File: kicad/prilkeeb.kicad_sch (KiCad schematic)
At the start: 71 parts, among them U2 Nice_Nano_V2

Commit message: Update layout
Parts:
- renumbered S3 to S1, S12 to S10, S13 to S11, S8 to S12, S9 to S13, S17 to S15, S18 to S16, S19 to S17, S20 to S18, S15 to S19, S4 to S2, S16 to S20, S24 to S22, S25 to S23, S26 to S24, S27 to S25, S22 to S26, S23 to S27, S5 to S3, S35 to S33, S33 to S35, S6 to S4, S1 to S5, S2 to S6, S10 to S8, S11 to S9
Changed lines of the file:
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@@
 		(dnp no)
 		(fields_autoplaced yes)
-		(property "Reference" "S5"
+		(property "Reference" "S3"
 			(at 96.52 73.66 0)
 			(do_not_autoplace yes)
@@
 			(project "nhienkeeb"
 				(path "/f238781f-c890-404f-bc9e-87ff6761e41b"
-					(reference "S5")
+					(reference "S3")
 					(unit 1)
 				)
@@
 		(dnp no)
 		(fields_autoplaced yes)
-		(property "Reference" "S6"
+		(property "Reference" "S4"
 			(at 111.76 73.66 0)
 			(do_not_autoplace yes)
@@
 			(project "nhienkeeb"
 				(path "/f238781f-c890-404f-bc9e-87ff6761e41b"
-					(reference "S6")
+					(reference "S4")
 					(unit 1)
 				)
@@
 		(dnp no)
 		(fields_autoplaced yes)
-		(property "Reference" "S24"
+		(property "Reference" "S22"
 			(at 67.31 119.38 0)
 			(do_not_autoplace yes)
@@
 			(project "nhienkeeb"
 				(path "/f238781f-c890-404f-bc9e-87ff6761e41b"
-					(reference "S24")
+					(reference "S22")
 					(unit 1)
 				)
@@
 		(dnp no)
 		(fields_autoplaced yes)
-		(property "Reference" "S22"
+		(property "Reference" "S26"
 			(at 39.37 119.38 0)
 			(do_not_autoplace yes)
@@
 			(project "nhienkeeb"
 				(path "/f238781f-c890-404f-bc9e-87ff6761e41b"
-					(reference "S22")
+					(reference "S26")
 					(unit 1)
 				)
@@
 		(on_board yes)
 		(dnp no)
-		(property "Reference" "S9"
+		(property "Reference" "S13"
 			(at 53.34 88.9 0)
 			(do_not_autoplace yes)
@@
 			(project "nhienkeeb"
 				(path "/f238781f-c890-404f-bc9e-87ff6761e41b"
-					(reference "S9")
+					(reference "S13")
 					(unit 1)
 				)
@@
 		(dnp no)
 		(fields_autoplaced yes)
-		(property "Reference" "S13"
+		(property "Reference" "S11"
 			(at 111.76 88.9 0)
 			(do_not_autoplace yes)
@@
 			(project "nhienkeeb"
 				(path "/f238781f-c890-404f-bc9e-87ff6761e41b"
-					(reference "S13")
+					(reference "S11")
 					(unit 1)
 				)
@@
 		(dnp no)
 		(fields_autoplaced yes)
-		(property "Reference" "S33"
+		(property "Reference" "S35"
 			(at 96.52 134.62 0)
 			(do_not_autoplace yes)
@@
 			(project "nhienkeeb"
 				(path "/f238781f-c890-404f-bc9e-87ff6761e41b"
-					(reference "S33")
+					(reference "S35")
 					(unit 1)
 				)
@@
 		(dnp no)
 		(fields_autoplaced yes)
-		(property "Reference" "S4"
+		(property "Reference" "S2"
 			(at 81.28 73.66 0)
 			(do_not_autoplace yes)
@@
 			(project "nhienkeeb"
 				(path "/f238781f-c890-404f-bc9e-87ff6761e41b"
-					(reference "S4")
+					(reference "S2")
 					(unit 1)
 				)
@@
 		(dnp no)
 		(fields_autoplaced yes)
-		(property "Reference" "S8"
+		(property "Reference" "S12"
 			(at 39.37 88.9 0)
 			(do_not_autoplace yes)
@@
 			(project "nhienkeeb"
 				(path "/f238781f-c890-404f-bc9e-87ff6761e41b"
-					(reference "S8")
+					(reference "S12")
 					(unit 1)
 				)
@@
 		(dnp no)
 		(fields_autoplaced yes)
-		(property "Reference" "S20"
+		(property "Reference" "S18"
 			(at 111.76 104.14 0)
 			(do_not_autoplace yes)
@@
 			(project "nhienkeeb"
 				(path "/f238781f-c890-404f-bc9e-87ff6761e41b"
-					(reference "S20")
+					(reference "S18")
 					(unit 1)
 				)
@@
 		(dnp no)
 		(fields_autoplaced yes)
-		(property "Reference" "S18"
+		(property "Reference" "S16"
 			(at 81.28 104.14 0)
 			(do_not_autoplace yes)
@@
 			(project "nhienkeeb"
 				(path "/f238781f-c890-404f-bc9e-87ff6761e41b"
-					(reference "S18")
+					(reference "S16")
 					(unit 1)
 				)
@@
 		(dnp no)
 		(fields_autoplaced yes)
-		(property "Reference" "S10"
+		(property "Reference" "S8"
 			(at 67.31 88.9 0)
 			(do_not_autoplace yes)
@@
 			(project "nhienkeeb"
 				(path "/f238781f-c890-404f-bc9e-87ff6761e41b"
-					(reference "S10")
+					(reference "S8")
 					(unit 1)
 				)
@@
 		(dnp no)
 		(fields_autoplaced yes)
-		(property "Reference" "S35"
+		(property "Reference" "S33"
 			(at 125.73 134.62 0)
 			(do_not_autoplace yes)
@@
 			(project "nhienkeeb"
 				(path "/f238781f-c890-404f-bc9e-87ff6761e41b"
-					(reference "S35")
+					(reference "S33")
 					(unit 1)
 				)
@@
 		(on_board yes)
 		(dnp no)
-		(property "Reference" "S23"
+		(property "Reference" "S27"
 			(at 53.34 119.38 0)
 			(do_not_autoplace yes)
@@
 			(project "nhienkeeb"
 				(path "/f238781f-c890-404f-bc9e-87ff6761e41b"
-					(reference "S23")
+					(reference "S27")
 					(unit 1)
 				)
@@
 		(dnp no)
 		(fields_autoplaced yes)
-		(property "Reference" "S17"
+		(property "Reference" "S15"
 			(at 67.31 104.14 0)
 			(do_not_autoplace yes)
@@
 			(project "nhienkeeb"
 				(path "/f238781f-c890-404f-bc9e-87ff6761e41b"
-					(reference "S17")
+					(reference "S15")
 					(unit 1)
 				)
@@
 		(dnp no)
 		(fields_autoplaced yes)
-		(property "Reference" "S12"
+		(property "Reference" "S10"
 			(at 96.52 88.9 0)
 			(do_not_autoplace yes)
@@
 			(project "nhienkeeb"
 				(path "/f238781f-c890-404f-bc9e-87ff6761e41b"
-					(reference "S12")
+					(reference "S10")
 					(unit 1)
 				)
@@
 		(dnp no)
 		(fields_autoplaced yes)
-		(property "Reference" "S25"
+		(property "Reference" "S23"
 			(at 81.28 119.38 0)
 			(do_not_autoplace yes)
@@
 			(project "nhienkeeb"
 				(path "/f238781f-c890-404f-bc9e-87ff6761e41b"
-					(reference "S25")
+					(reference "S23")
 					(unit 1)
 				)
@@
 		(on_board yes)
 		(dnp no)
-		(property "Reference" "S16"
+		(property "Reference" "S20"
 			(at 53.34 104.14 0)
 			(do_not_autoplace yes)
@@
 			(project "nhienkeeb"
 				(path "/f238781f-c890-404f-bc9e-87ff6761e41b"
-					(reference "S16")
+					(reference "S20")
 					(unit 1)
 				)
@@
 		(dnp no)
 		(fields_autoplaced yes)
-		(property "Reference" "S15"
+		(property "Reference" "S19"
 			(at 39.37 104.14 0)
 			(do_not_autoplace yes)
@@
 			(project "nhienkeeb"
 				(path "/f238781f-c890-404f-bc9e-87ff6761e41b"
-					(reference "S15")
+					(reference "S19")
 					(unit 1)
 				)
@@
 		(dnp no)
 		(fields_autoplaced yes)
-		(property "Reference" "S27"
+		(property "Reference" "S25"
 			(at 111.76 119.38 0)
 			(do_not_autoplace yes)
@@
 			(project "nhienkeeb"
 				(path "/f238781f-c890-404f-bc9e-87ff6761e41b"
-					(reference "S27")
+					(reference "S25")
 					(unit 1)
 				)
@@
 		(dnp no)
 		(fields_autoplaced yes)
-		(property "Reference" "S1"
+		(property "Reference" "S5"
 			(at 39.37 73.66 0)
 			(do_not_autoplace yes)
@@
 			(project ""
 				(path "/f238781f-c890-404f-bc9e-87ff6761e41b"
-					(reference "S1")
+					(reference "S5")
 					(unit 1)
 				)
@@
 		(dnp no)
 		(fields_autoplaced yes)
-		(property "Reference" "S19"
+		(property "Reference" "S17"
 			(at 96.52 104.14 0)
 			(do_not_autoplace yes)
@@
 			(project "nhienkeeb"
 				(path "/f238781f-c890-404f-bc9e-87ff6761e41b"
-					(reference "S19")
+					(reference "S17")
 					(unit 1)
 				)
@@
 		(dnp no)
 		(fields_autoplaced yes)
-		(property "Reference" "S3"
+		(property "Reference" "S1"
 			(at 67.31 73.66 0)
 			(do_not_autoplace yes)
@@
 			(project "nhienkeeb"
 				(path "/f238781f-c890-404f-bc9e-87ff6761e41b"
-					(reference "S3")
+					(reference "S1")
 					(unit 1)
 				)
@@
 		(dnp no)
 		(fields_autoplaced yes)
-		(property "Reference" "S26"
+		(property "Reference" "S24"
 			(at 96.52 119.38 0)
 			(do_not_autoplace yes)
@@
 			(project "nhienkeeb"
 				(path "/f238781f-c890-404f-bc9e-87ff6761e41b"
-					(reference "S26")
+					(reference "S24")
 					(unit 1)
 				)
@@
 		(dnp no)
 		(fields_autoplaced yes)
-		(property "Reference" "S11"
+		(property "Reference" "S9"
 			(at 81.28 88.9 0)
 			(do_not_autoplace yes)
@@
 			(project "nhienkeeb"
 				(path "/f238781f-c890-404f-bc9e-87ff6761e41b"
-					(reference "S11")
+					(reference "S9")
 					(unit 1)
 				)
@@
 		(on_board yes)
 		(dnp no)
-		(property "Reference" "S2"
+		(property "Reference" "S6"
 			(at 53.34 73.66 0)
 			(do_not_autoplace yes)
@@
 			(project "nhienkeeb"
 				(path "/f238781f-c890-404f-bc9e-87ff6761e41b"
-					(reference "S2")
+					(reference "S6")
 					(unit 1)
 				)

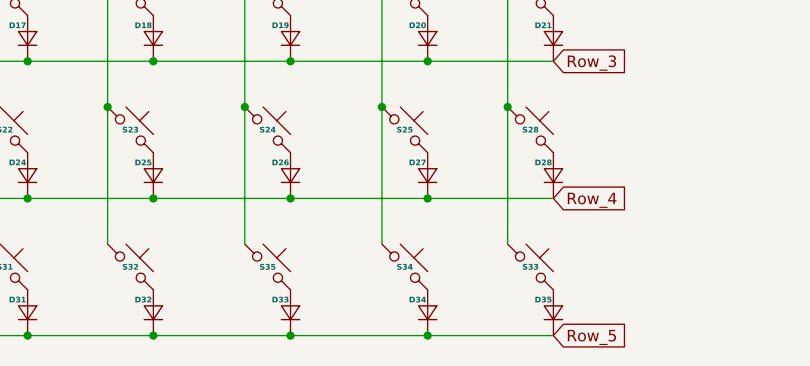
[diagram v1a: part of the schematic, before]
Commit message: Update placement and basice routing
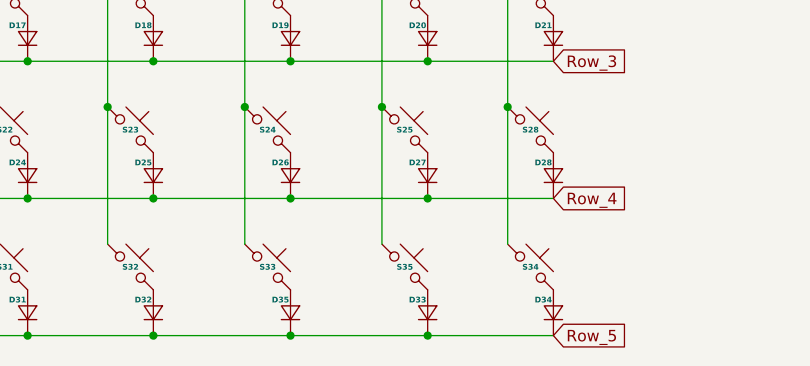
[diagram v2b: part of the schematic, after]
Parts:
- renumbered D34 to D33, D35 to D34, D33 to D35, S35 to S33, S33 to S34, S34 to S35
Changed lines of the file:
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@@
 		(dnp no)
 		(fields_autoplaced yes)
-		(property "Reference" "D34"
+		(property "Reference" "D33"
 			(at 114.15 138.634 0)
 			(do_not_autoplace yes)
@@
 			(project "nhienkeeb"
 				(path "/f238781f-c890-404f-bc9e-87ff6761e41b"
-					(reference "D34")
+					(reference "D33")
 					(unit 1)
 				)
@@
 		(dnp no)
 		(fields_autoplaced yes)
-		(property "Reference" "S35"
+		(property "Reference" "S33"
 			(at 96.52 134.62 0)
 			(do_not_autoplace yes)
@@
 			(project "nhienkeeb"
 				(path "/f238781f-c890-404f-bc9e-87ff6761e41b"
-					(reference "S35")
+					(reference "S33")
 					(unit 1)
 				)
@@
 		(dnp no)
 		(fields_autoplaced yes)
-		(property "Reference" "S33"
+		(property "Reference" "S34"
 			(at 125.73 134.62 0)
 			(do_not_autoplace yes)
@@
 			(project "nhienkeeb"
 				(path "/f238781f-c890-404f-bc9e-87ff6761e41b"
-					(reference "S33")
+					(reference "S34")
 					(unit 1)
 				)
@@
 		(dnp no)
 		(fields_autoplaced yes)
-		(property "Reference" "S34"
+		(property "Reference" "S35"
 			(at 111.76 134.62 0)
 			(do_not_autoplace yes)
@@
 			(project "nhienkeeb"
 				(path "/f238781f-c890-404f-bc9e-87ff6761e41b"
-					(reference "S34")
+					(reference "S35")
 					(unit 1)
 				)
@@
 		(dnp no)
 		(fields_autoplaced yes)
-		(property "Reference" "D33"
+		(property "Reference" "D35"
 			(at 98.91 138.634 0)
 			(do_not_autoplace yes)
@@
 			(project "nhienkeeb"
 				(path "/f238781f-c890-404f-bc9e-87ff6761e41b"
-					(reference "D33")
+					(reference "D35")
 					(unit 1)
 				)
@@
 		(dnp no)
 		(fields_autoplaced yes)
-		(property "Reference" "D35"
+		(property "Reference" "D34"
 			(at 128.12 138.634 0)
 			(do_not_autoplace yes)
@@
 			(project "nhienkeeb"
 				(path "/f238781f-c890-404f-bc9e-87ff6761e41b"
-					(reference "D35")
-					(unit 1)
-				)
+					(reference "D34")
+					(unit 1)
+				)

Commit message: Update layout
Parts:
- renumbered S35 to S32, S34 to S33, S32 to S34, S33 to S35
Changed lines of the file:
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@@
 		(dnp no)
 		(fields_autoplaced yes)
-		(property "Reference" "S33"
+		(property "Reference" "S35"
 			(at 96.52 134.62 0)
 			(do_not_autoplace yes)
@@
 			(project "nhienkeeb"
 				(path "/f238781f-c890-404f-bc9e-87ff6761e41b"
-					(reference "S33")
+					(reference "S35")
 					(unit 1)
 				)
@@
 		(dnp no)
 		(fields_autoplaced yes)
-		(property "Reference" "S34"
+		(property "Reference" "S33"
 			(at 125.73 134.62 0)
 			(do_not_autoplace yes)
@@
 			(project "nhienkeeb"
 				(path "/f238781f-c890-404f-bc9e-87ff6761e41b"
-					(reference "S34")
+					(reference "S33")
 					(unit 1)
 				)
@@
 		(dnp no)
 		(fields_autoplaced yes)
-		(property "Reference" "S35"
+		(property "Reference" "S32"
 			(at 111.76 134.62 0)
 			(do_not_autoplace yes)
@@
 			(project "nhienkeeb"
 				(path "/f238781f-c890-404f-bc9e-87ff6761e41b"
-					(reference "S35")
+					(reference "S32")
 					(unit 1)
 				)
@@
 		(dnp no)
 		(fields_autoplaced yes)
-		(property "Reference" "S32"
+		(property "Reference" "S34"
 			(at 81.28 134.62 0)
 			(do_not_autoplace yes)
@@
 			(project "nhienkeeb"
 				(path "/f238781f-c890-404f-bc9e-87ff6761e41b"
-					(reference "S32")
-					(unit 1)
-				)
+					(reference "S34")
+					(unit 1)
+				)

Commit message: Update layout
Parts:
- renumbered S35 to S32, S32 to S33, S33 to S34, S34 to S35
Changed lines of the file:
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@@
 		(dnp no)
 		(fields_autoplaced yes)
-		(property "Reference" "S35"
+		(property "Reference" "S32"
 			(at 96.52 134.62 0)
 			(do_not_autoplace yes)
@@
 			(project "nhienkeeb"
 				(path "/f238781f-c890-404f-bc9e-87ff6761e41b"
-					(reference "S35")
+					(reference "S32")
 					(unit 1)
 				)
@@
 		(dnp no)
 		(fields_autoplaced yes)
-		(property "Reference" "S33"
+		(property "Reference" "S34"
 			(at 125.73 134.62 0)
 			(do_not_autoplace yes)
@@
 			(project "nhienkeeb"
 				(path "/f238781f-c890-404f-bc9e-87ff6761e41b"
-					(reference "S33")
+					(reference "S34")
 					(unit 1)
 				)
@@
 		(dnp no)
 		(fields_autoplaced yes)
-		(property "Reference" "S32"
+		(property "Reference" "S33"
 			(at 111.76 134.62 0)
 			(do_not_autoplace yes)
@@
 			(project "nhienkeeb"
 				(path "/f238781f-c890-404f-bc9e-87ff6761e41b"
-					(reference "S32")
+					(reference "S33")
 					(unit 1)
 				)
@@
 		(dnp no)
 		(fields_autoplaced yes)
-		(property "Reference" "S34"
+		(property "Reference" "S35"
 			(at 81.28 134.62 0)
 			(do_not_autoplace yes)
@@
 			(project "nhienkeeb"
 				(path "/f238781f-c890-404f-bc9e-87ff6761e41b"
-					(reference "S34")
-					(unit 1)
-				)
+					(reference "S35")
+					(unit 1)
+				)

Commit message: Update design
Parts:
- added RST_SW_L1, RST_SW_R1: SW_Push, Button_Switch_SMD:SW_SPST_SKQG_WithStem, symbol Switch:SW_Push
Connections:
- net VCC: now reaches U2.21 (3.3v)
- net RST: now reaches U2.22 (RST)
- net RST: now also RST_SW_L1.2, RST_SW_R1.2
- net GND: now reaches U2.23 (GND)
- net GND: now also RST_SW_L1.1, RST_SW_R1.1

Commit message: Design checkpoint
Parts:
- removed RST_SW_R1: SW_Push, Button_Switch_SMD:SW_SPST_SKQG_WithStem, symbol Switch:SW_Push
- removed S34: S35, key-switches:SW_MX_HotSwap_PTH_double, symbol ScottoKeebs:Placeholder_Keyswitch
- added BT1: Battery_Cell, dumta:Battery_pads_reversible, symbol Device:Battery_Cell
- added ROT1: RotaryEncoder_Switch_MP, ScottoKeebs_Scotto:Encoder_EC11_MX, symbol Device:RotaryEncoder_Switch_MP
- added SW1: SW_SPDT, dumta:power_switch_padreverse, symbol Switch:SW_SPDT
- RST_SW1: renamed from RST_SW_L1; footprint Button_Switch_SMD:SW_SPST_SKQG_WithStem -> Button_Switch_THT:SW_PUSH_6mm_H4.3mm
- renumbered D35 to D33, D33 to D34, D34 to DROTARY1, S35 to S34
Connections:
- net Col_7: now also ROT1.S2
- net RotaryA: now reaches U2.11 (8)
- net RotaryA: now also ROT1.A
- net RotaryB: now reaches U2.12 (9)
- net RotaryB: now also ROT1.B
- net at DROTARY1.2 (A): now also ROT1.S1
- new net: BT1.1 (+), SW1.2 (B)
- new net B+: SW1.3 (C), U2.29 (B+)
- new net B-: BT1.2 (-), U2.28 (B-)

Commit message: Update components
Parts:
- added RST_SW2: SW_Push, ScottoKeebs_Components:Button_TL3342, symbol Switch:SW_Push
- ROT1: footprint ScottoKeebs_Scotto:Encoder_EC11_MX -> prillkeeb:Encoder_EC11_MX_Jumpers_Reversible
- RST_SW1: footprint Button_Switch_THT:SW_PUSH_6mm_H4.3mm -> ScottoKeebs_Components:Button_TL3342
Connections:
- net GND: now also RST_SW2.1
- net RST: now also RST_SW2.2
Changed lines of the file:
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@@
 		)
 	)
+	(global_label "RST"
+		(shape input)
+		(at 200.66 68.58 0)
+		(fields_autoplaced yes)
+		(effects
+			(font
+				(size 1.27 1.27)
+			)
+			(justify left)
+		)
+		(property "Intersheetrefs" "${INTERSHEET_REFS}"
+			(at 207.0923 68.58 0)
+			(effects
+				(font
+					(size 1.27 1.27)
+				)
+				(justify left)
+				(hide yes)
+			)
+		)
+	)
 	(global_label "Col_5"
 		(shape input)
@@
 		)
 	)
+	(global_label "GND"
+		(shape input)
+		(at 190.5 68.58 180)
+		(fields_autoplaced yes)
+		(effects
+			(font
+				(size 1.27 1.27)
+			)
+			(justify right)
+		)
+		(property "Intersheetrefs" "${INTERSHEET_REFS}"
+			(at 183.6443 68.58 0)
+			(effects
+				(font
+					(size 1.27 1.27)
+				)
+				(justify right)
+				(hide yes)
+			)
+		)
+	)
 	(global_label "Col_2"
 		(shape input)
@@
 		(pin "19"
 		)
-		(pin "RAW"
+		(pin "24"
 		)
 		(pin "18"
@@
 			)
 		)
-		(property "Footprint" "Button_Switch_THT:SW_PUSH_6mm_H4.3mm"
+		(property "Footprint" "ScottoKeebs_Components:Button_TL3342"
 			(at 195.58 50.8 0)
 			(effects
@@
 			)
 		)
-		(property "Footprint" "ScottoKeebs_Scotto:Encoder_EC11_MX"
+		(property "Footprint" "prillkeeb:Encoder_EC11_MX_Jumpers_Reversible"
 			(at 151.384 125.73 0)
 			(effects
@@
 					(unit 1)
 				)
+			)
+		)
+	)
+	(symbol
+		(lib_id "Switch:SW_Push")
+		(at 195.58 68.58 0)
+		(unit 1)
+		(exclude_from_sim no)
+		(in_bom yes)
+		(on_board yes)
+		(dnp no)
+		(fields_autoplaced yes)
+		(property "Reference" "RST_SW2"
+			(at 195.58 60.96 0)
+			(effects
+				(font
+					(size 1.27 1.27)
+				)
+			)
+		)
+		(property "Value" "SW_Push"
+			(at 195.58 63.5 0)
+			(effects
+				(font
+					(size 1.27 1.27)
+				)
+			)
+		)
+		(property "Footprint" "ScottoKeebs_Components:Button_TL3342"
+			(at 195.58 63.5 0)
+			(effects
+				(font
+					(size 1.27 1.27)
+				)
+				(hide yes)
+			)
+		)
+		(property "Datasheet" "~"
+			(at 195.58 63.5 0)
+			(effects
+				(font
+					(size 1.27 1.27)
+				)
+				(hide yes)
+			)
+		)
+		(property "Description" "Push button switch, generic, two pins"
+			(at 195.58 68.58 0)
+			(effects
+				(font
+					(size 1.27 1.27)
+				)
+				(hide yes)
+			)
+		)
+		(pin "2"
+		)
+		(pin "1"
+		)
+		(instances
+			(project "prilkeeb"
+				(path "/f238781f-c890-404f-bc9e-87ff6761e41b"
+					(reference "RST_SW2")
+					(unit 1)
+				)

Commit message: Routing
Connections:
- net GND: now also ROT1.C
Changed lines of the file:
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@@
+		)
+	)
+	(global_label "GND"
+		(shape input)
+		(at 147.32 121.92 90)
+		(fields_autoplaced yes)
+		(effects
+			(font
+				(size 1.27 1.27)
+			)
+			(justify left)
+		)
+		(property "Intersheetrefs" "${INTERSHEET_REFS}"
+			(at 147.32 115.0643 90)
+			(effects
+				(font
+					(size 1.27 1.27)
+				)
+				(justify left)
+				(hide yes)
+			)
 		)
 	)
